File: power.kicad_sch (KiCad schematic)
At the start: 39 parts, among them J501 PJ-002AH-SMT-TR, Q501 SI2371EDS-T1-GE3, U501 TPS5402, U502 TLV1117-50, U503 MIC5317-3.3YM5-TR

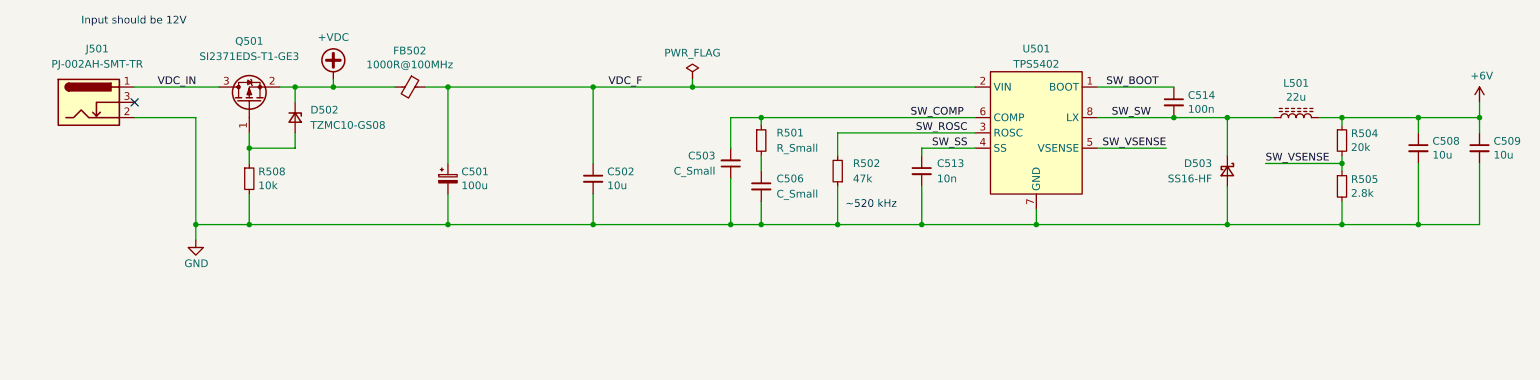
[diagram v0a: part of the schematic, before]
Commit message: Complete power supply design
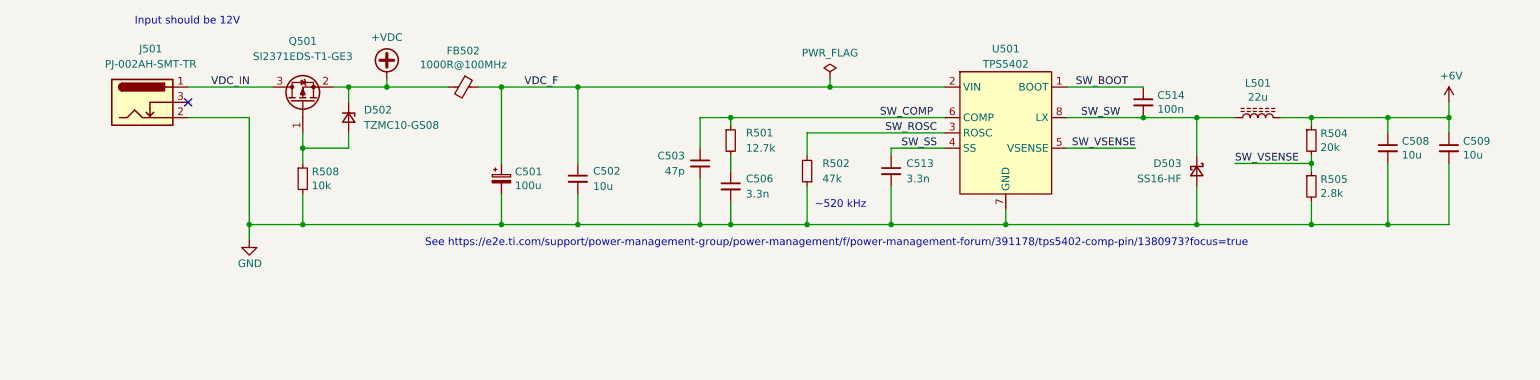
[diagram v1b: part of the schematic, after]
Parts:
- C503: value C_Small -> 47p; PN (none) -> 885012007014
- C506: value C_Small -> 3.3n; PN (none) -> C2012C0G2A332J125AA
- C513: value 10n -> 3.3n; PN (none) -> C2012C0G2A332J125AA
- R501: value R_Small -> 12.7k; PN (none) -> CR0805-FX-1272ELF
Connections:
- net GND: now also C503.2; no longer C503.1
- net SW_COMP: now also C503.1; no longer C503.2
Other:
- note added: "See https://e2e.ti.com/support/power-management-group/power-management/f/power-management-forum/391178/tps5402-comp-pin/1380973?focus=true"
- moved on the sheet: C501, C502, C506, C508, C509, C514, D502, D503, FB502, J501, L501, Q501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

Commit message: Ready for layout
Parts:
- L501: footprint (none) -> Inductor_SMD:L_Taiyo-Yuden_NR-50xx_HandSoldering
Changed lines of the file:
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@@
     (property "Reference" "L501" (id 0) (at 228.6 29.845 90))
     (property "Value" "22u" (id 1) (at 228.6 32.1564 90))
-    (property "Footprint" "" (id 2) (at 228.6 35.56 0)
+    (property "Footprint" "Inductor_SMD:L_Taiyo-Yuden_NR-50xx_HandSoldering" (id 2) (at 228.6 35.56 0)
       (effects (font (size 1.27 1.27)) hide)
     )

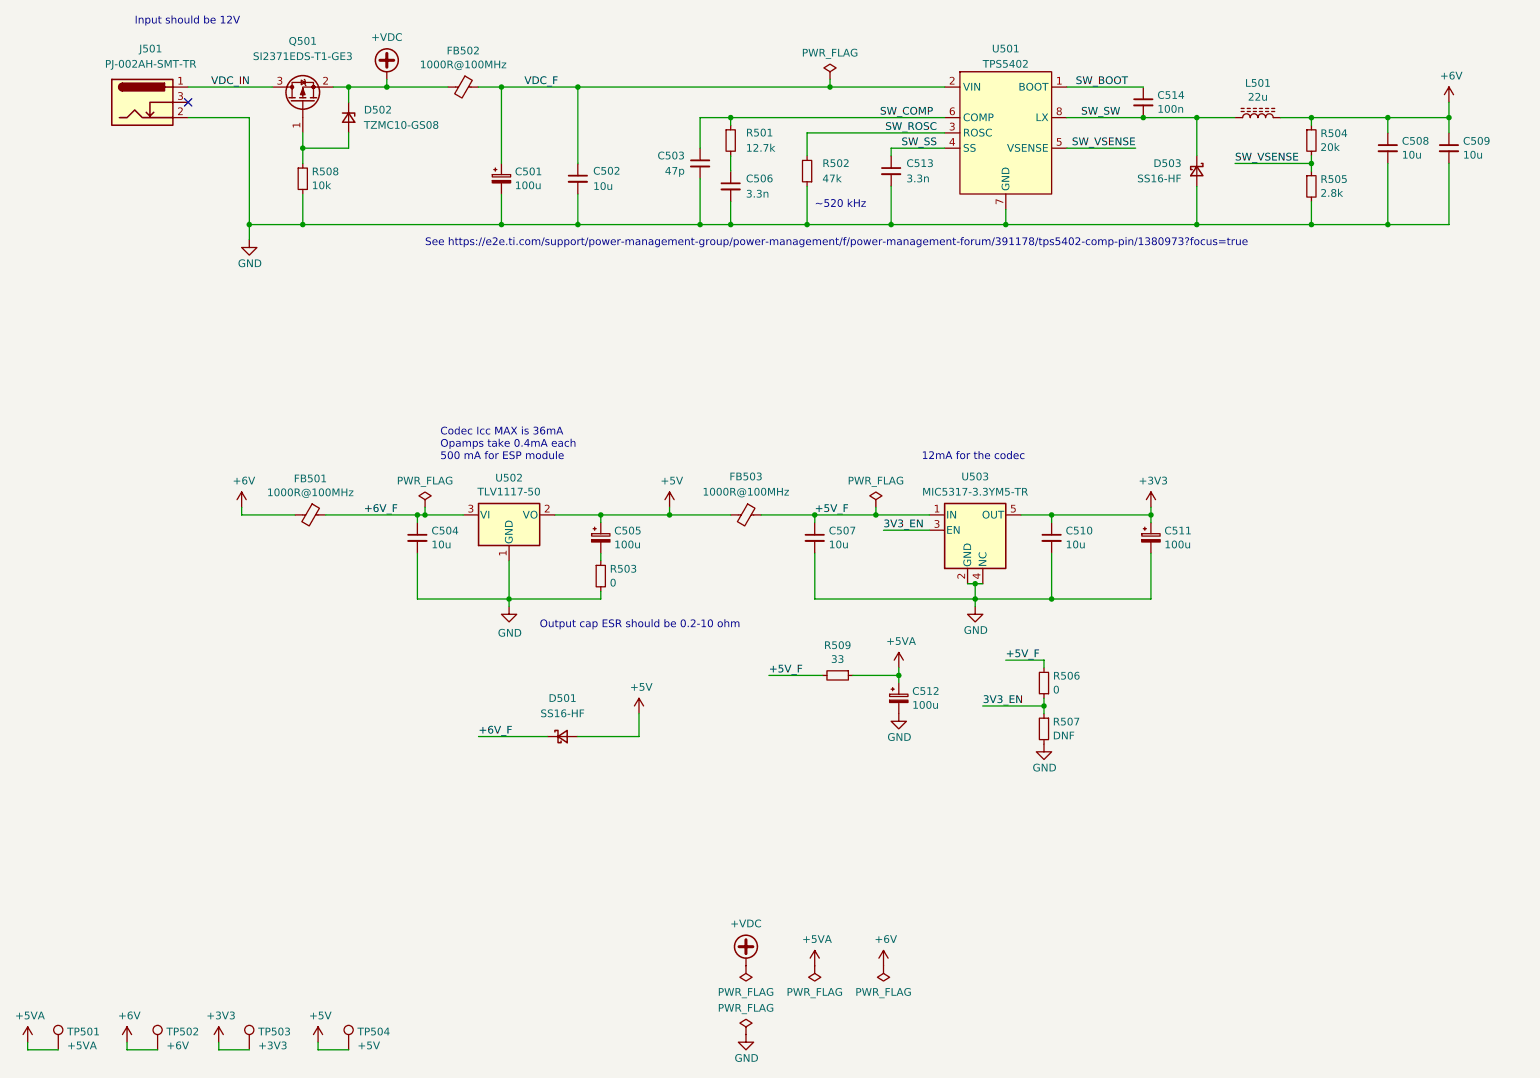
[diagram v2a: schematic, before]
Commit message: Clean up layout, add testpoints, layer markers
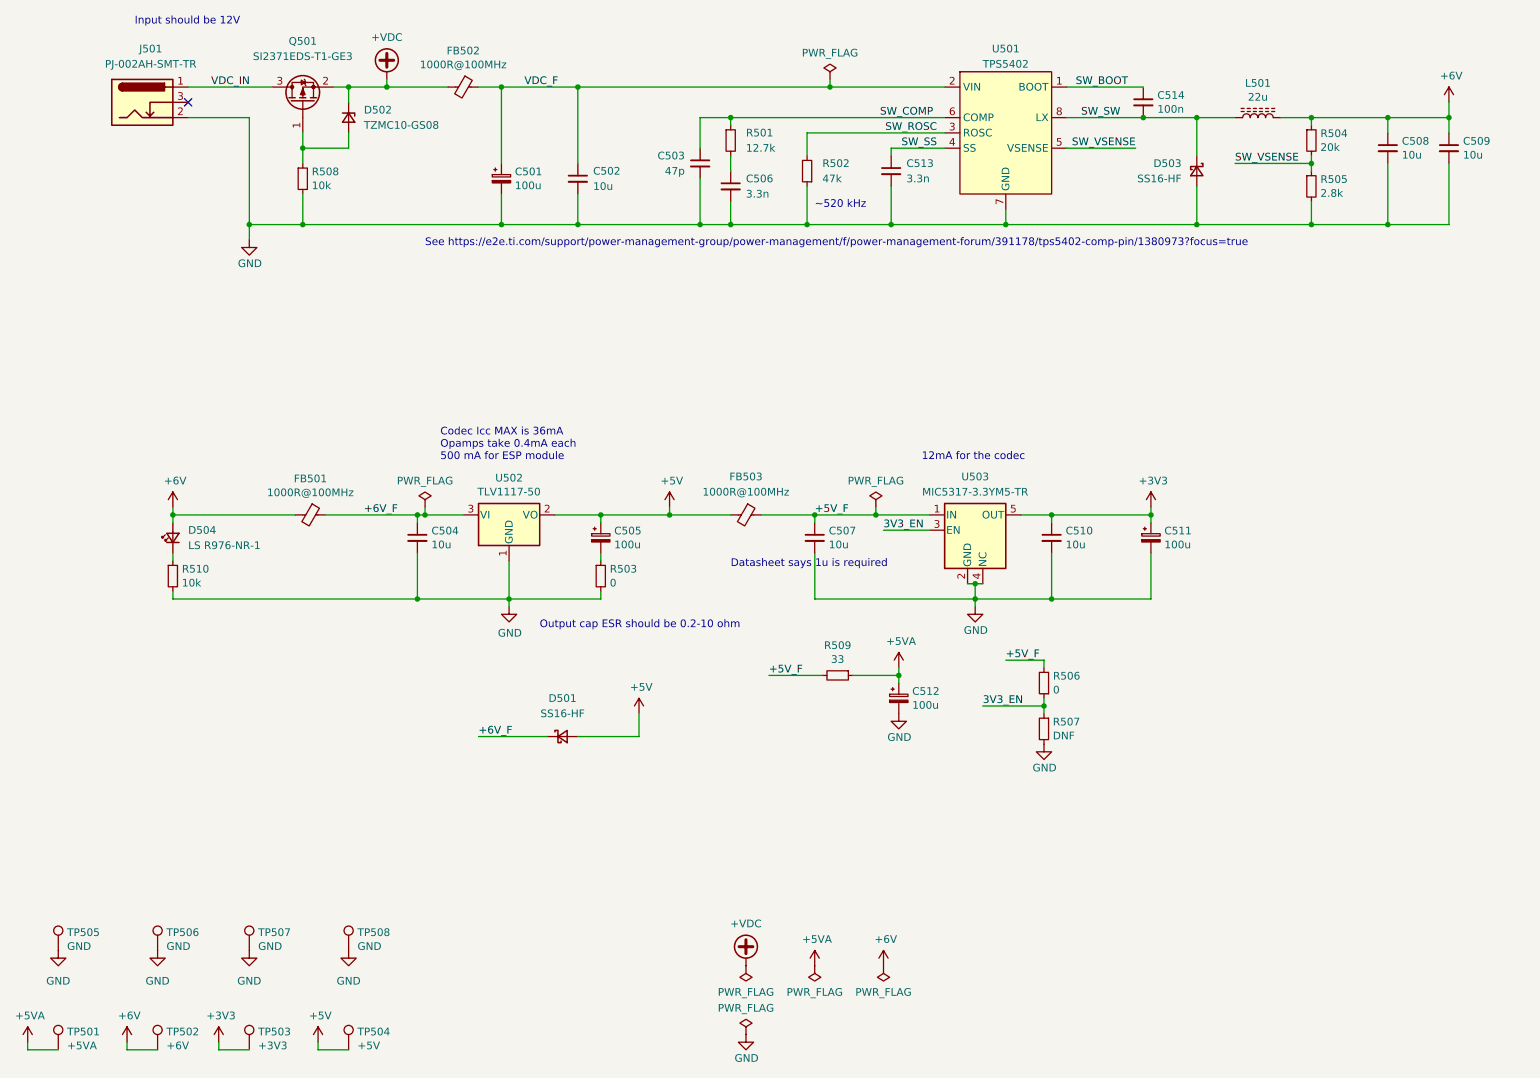
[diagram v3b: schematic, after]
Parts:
- added D504: LS R976-NR-1, LED_SMD:LED_0805_2012Metric_Castellated, symbol Device:LED_Small
- added R510: 10k, Resistor_SMD:R_0805_2012Metric_Pad1.20x1.40mm_HandSolder, symbol Device:R_Small
- added TP505, TP506, TP507, TP508: GND, guitar_dsp_platform:TestPoint_THTPad_D2.0mm_Drill1.0mm, symbol Connector:TestPoint
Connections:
- net +6V: now also D504.2 (A)
- net GND: now also R510.2, TP505.1, TP506.1, TP507.1, TP508.1
- new net: D504.1 (K), R510.1
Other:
- note added: "Datasheet says 1u is required"

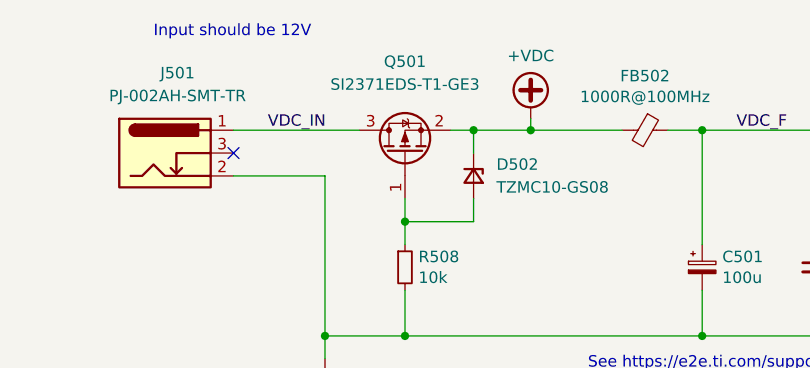
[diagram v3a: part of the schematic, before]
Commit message: Final BOM changes
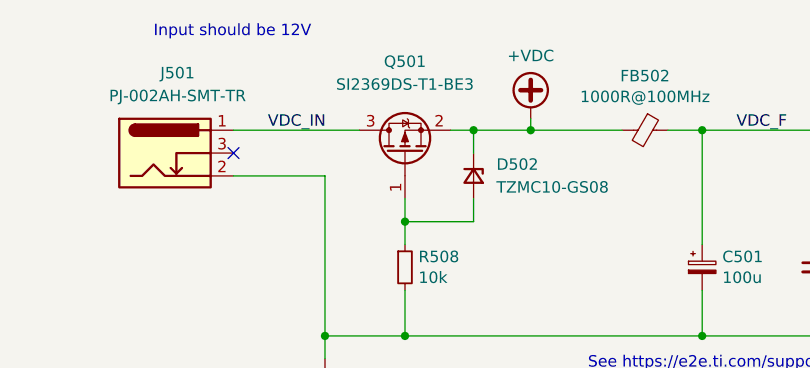
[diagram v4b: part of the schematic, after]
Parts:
- C501, C505, C511, C512: footprint Capacitor_SMD:CP_Elec_6.3x5.8 -> Capacitor_SMD:CP_Elec_6.3x7.7; PN EEEFK1E101SP -> EEE1EA101XAP
- Q501: value SI2371EDS-T1-GE3 -> SI2369DS-T1-BE3; PN SI2371EDS-T1-GE3 -> SI2369DS-T1-BE3
- U501: PN (none) -> TPS5402DR
- U502: PN TLV1117-15CDCY -> TLV1117-50IDCYR
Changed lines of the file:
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@@
       (effects (font (size 1.27 1.27)) (justify left))
     )
-    (property "Footprint" "Capacitor_SMD:CP_Elec_6.3x5.8" (id 2) (at 102.87 45.72 0)
-      (effects (font (size 1.27 1.27)) hide)
-    )
-    (property "Datasheet" "https://www.mouser.co.uk/datasheet/2/315/ABA0000C1251-1138508.pdf" (id 3) (at 102.87 45.72 0)
-      (effects (font (size 1.27 1.27)) hide)
-    )
-    (property "PN" "EEEFK1E101SP" (id 4) (at 102.87 45.72 0)
+    (property "Footprint" "Capacitor_SMD:CP_Elec_6.3x7.7" (id 2) (at 102.87 45.72 0)
+      (effects (font (size 1.27 1.27)) hide)
+    )
+    (property "Datasheet" "https://www.mouser.co.uk/datasheet/2/315/ABA0000C1142-947446.pdf" (id 3) (at 102.87 45.72 0)
+      (effects (font (size 1.27 1.27)) hide)
+    )
+    (property "PN" "EEE1EA101XAP" (id 4) (at 102.87 45.72 0)
       (effects (font (size 1.27 1.27)) hide)
     )
@@
       (effects (font (size 1.27 1.27)) (justify left))
     )
-    (property "Footprint" "Capacitor_SMD:CP_Elec_6.3x5.8" (id 2) (at 119.38 105.41 0)
-      (effects (font (size 1.27 1.27)) hide)
-    )
-    (property "Datasheet" "https://www.mouser.co.uk/datasheet/2/315/ABA0000C1251-1138508.pdf" (id 3) (at 119.38 105.41 0)
-      (effects (font (size 1.27 1.27)) hide)
-    )
-    (property "PN" "EEEFK1E101SP" (id 4) (at 119.38 105.41 0)
+    (property "Footprint" "Capacitor_SMD:CP_Elec_6.3x7.7" (id 2) (at 119.38 105.41 0)
+      (effects (font (size 1.27 1.27)) hide)
+    )
+    (property "Datasheet" "https://www.mouser.co.uk/datasheet/2/315/ABA0000C1142-947446.pdf" (id 3) (at 119.38 105.41 0)
+      (effects (font (size 1.27 1.27)) hide)
+    )
+    (property "PN" "EEE1EA101XAP" (id 4) (at 119.38 105.41 0)
       (effects (font (size 1.27 1.27)) hide)
     )
@@
       (effects (font (size 1.27 1.27)) (justify left))
     )
-    (property "Footprint" "Capacitor_SMD:CP_Elec_6.3x5.8" (id 2) (at 168.91 132.08 0)
-      (effects (font (size 1.27 1.27)) hide)
-    )
-    (property "Datasheet" "https://www.mouser.co.uk/datasheet/2/315/ABA0000C1251-1138508.pdf" (id 3) (at 168.91 132.08 0)
-      (effects (font (size 1.27 1.27)) hide)
-    )
-    (property "PN" "EEEFK1E101SP" (id 4) (at 168.91 132.08 0)
+    (property "Footprint" "Capacitor_SMD:CP_Elec_6.3x7.7" (id 2) (at 168.91 132.08 0)
+      (effects (font (size 1.27 1.27)) hide)
+    )
+    (property "Datasheet" "https://www.mouser.co.uk/datasheet/2/315/ABA0000C1142-947446.pdf" (id 3) (at 168.91 132.08 0)
+      (effects (font (size 1.27 1.27)) hide)
+    )
+    (property "PN" "EEE1EA101XAP" (id 4) (at 168.91 132.08 0)
       (effects (font (size 1.27 1.27)) hide)
     )
@@
       (effects (font (size 1.27 1.27)) (justify left))
     )
-    (property "Footprint" "Capacitor_SMD:CP_Elec_6.3x5.8" (id 2) (at 210.82 105.41 0)
-      (effects (font (size 1.27 1.27)) hide)
-    )
-    (property "Datasheet" "https://www.mouser.co.uk/datasheet/2/315/ABA0000C1251-1138508.pdf" (id 3) (at 210.82 105.41 0)
-      (effects (font (size 1.27 1.27)) hide)
-    )
-    (property "PN" "EEEFK1E101SP" (id 4) (at 210.82 105.41 0)
+    (property "Footprint" "Capacitor_SMD:CP_Elec_6.3x7.7" (id 2) (at 210.82 105.41 0)
+      (effects (font (size 1.27 1.27)) hide)
+    )
+    (property "Datasheet" "https://www.mouser.co.uk/datasheet/2/315/ABA0000C1142-947446.pdf" (id 3) (at 210.82 105.41 0)
+      (effects (font (size 1.27 1.27)) hide)
+    )
+    (property "PN" "EEE1EA101XAP" (id 4) (at 210.82 105.41 0)
       (effects (font (size 1.27 1.27)) hide)
     )
@@
     (in_bom yes) (on_board yes) (fields_autoplaced)
     (property "Reference" "Q501" (id 0) (at 69.85 22.86 90))
-    (property "Value" "SI2371EDS-T1-GE3" (id 1) (at 69.85 25.4 90))
+    (property "Value" "SI2369DS-T1-BE3" (id 1) (at 69.85 25.4 90))
     (property "Footprint" "Package_TO_SOT_SMD:SOT-23" (id 2) (at 67.31 27.94 0)
       (effects (font (size 1.27 1.27)) hide)
     )
-    (property "Datasheet" "https://www.mouser.co.uk/datasheet/2/427/VISH_S_A0010613187_1-2571006.pdf" (id 3) (at 69.85 33.02 0)
-      (effects (font (size 1.27 1.27)) hide)
-    )
-    (property "PN" "SI2371EDS-T1-GE3" (id 4) (at 69.85 33.02 90)
+    (property "Datasheet" "https://www.mouser.co.uk/datasheet/2/427/si2369d-1764360.pdf" (id 3) (at 69.85 33.02 0)
+      (effects (font (size 1.27 1.27)) hide)
+    )
+    (property "PN" "SI2369DS-T1-BE3" (id 4) (at 69.85 33.02 90)
       (effects (font (size 1.27 1.27)) hide)
     )
@@
       (effects (font (size 1.27 1.27)) hide)
     )
-    (property "PN" "TLV1117-15CDCY" (id 4) (at 104.14 101.6 0)
+    (property "PN" "TLV1117-50IDCYR" (id 4) (at 104.14 101.6 0)
       (effects (font (size 1.27 1.27)) hide)
     )
@@
       (effects (font (size 1.27 1.27)) hide)
     )
+    (property "PN" "TPS5402DR" (id 4) (at 186.69 34.29 0)
+      (effects (font (size 1.27 1.27)) hide)
+    )
